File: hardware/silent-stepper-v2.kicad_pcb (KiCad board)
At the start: 4 copper layers, 80 x 80 mm, 112 parts, among them P1 VIN, P101 CON-SENSOR2, P102 DEBUG, P103 BOOT, P2 OUT, P3 GPIO, P4 PROTO, Q1 CSD19533Q5A, Q2 CSD19533Q5A, Q3 CSD19533Q5A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

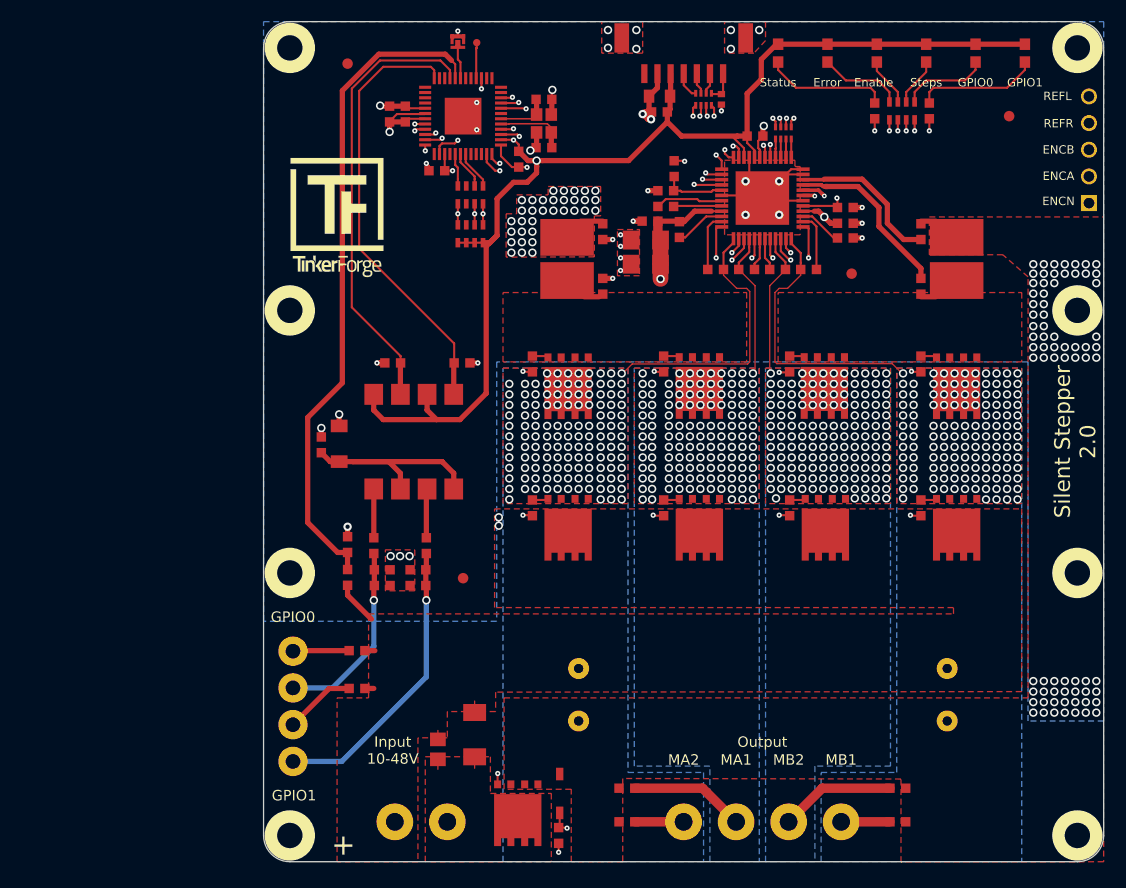
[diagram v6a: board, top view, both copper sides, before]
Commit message: changed shunt resistors
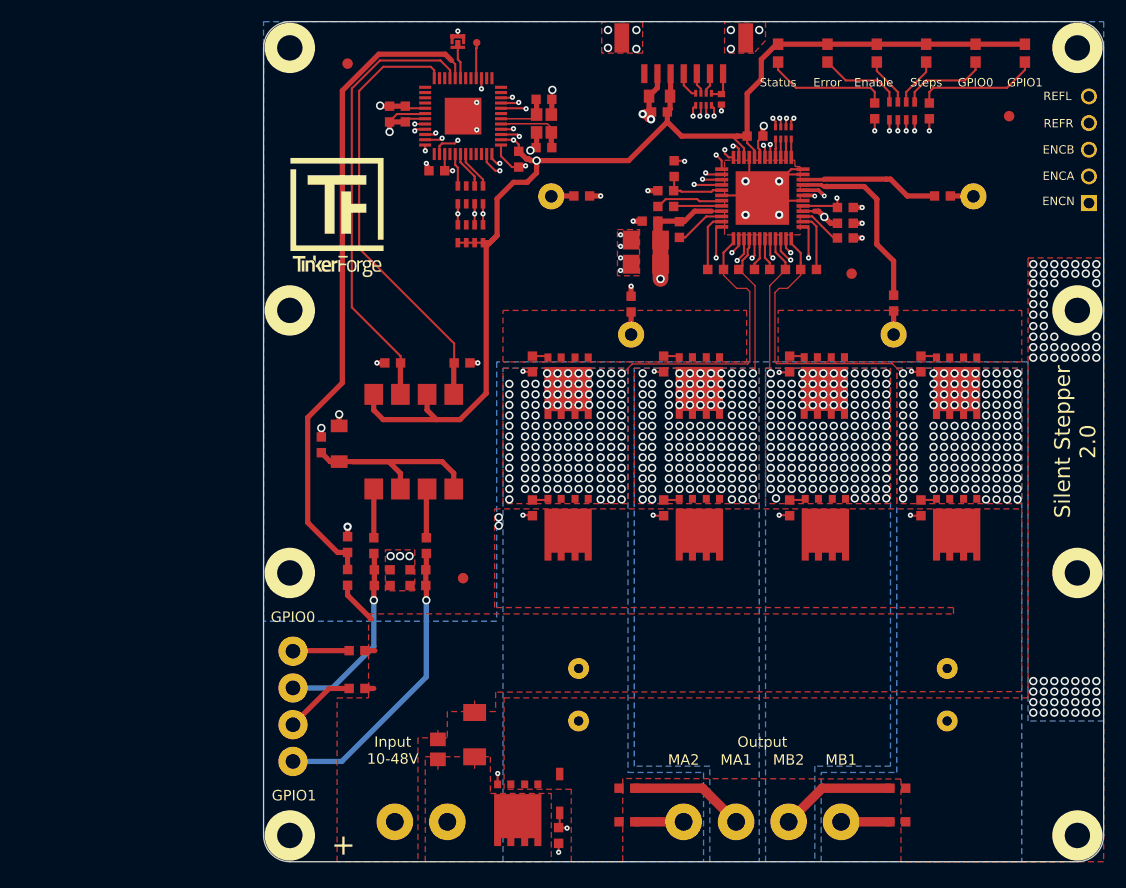
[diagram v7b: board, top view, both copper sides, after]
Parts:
- R10: value WSHM2818R0220FEA -> MRS-3; footprint kicad-libraries:R2818 -> kicad-libraries:MSR-3
- R11: value WSHM2818R0220FEA -> MRS_-3; footprint kicad-libraries:R2818 -> kicad-libraries:MSR-3
- moved R7 3.97 mm to (109.7, 106.6), turned to 180 degrees
- moved R9 3.94 mm to (75.3, 106.6), turned to 0 degrees
- moved R8 3.19 mm to (80.0, 116.9)
- moved R6 3.05 mm to (105.0, 116.8)
- moved R11 2.38 mm to (76.2, 113.2), turned to 300 degrees
- moved R10 2.29 mm to (108.8, 113.2), turned to 240 degrees
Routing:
- net GND: track 67.7 -> 61.5 mm, vias 145 -> 112
- net V_GPIO: track 94.0 -> 97.0 mm
- net Net-(R2-Pad2): track 33.8 -> 36.7 mm
- net Net-(R3-Pad2): track 18.6 -> 21.2 mm
- net Net-(Q4-PadS): track 4.23 -> 2.15 mm
- net Net-(Q2-PadS): track 4.23 -> 2.25 mm
- net Net-(R15-Pad2): track 27.1 -> 28.7 mm
- net Net-(R14-Pad2): track 41.8 -> 43.4 mm
- net Net-(R7-Pad2): track 14.7 -> 13.2 mm
- net Net-(R8-Pad2): track 26.8 -> 25.4 mm
- net Net-(R6-Pad2): track 16.7 -> 17.6 mm
- net Net-(R9-Pad2): track 23.5 -> 22.8 mm

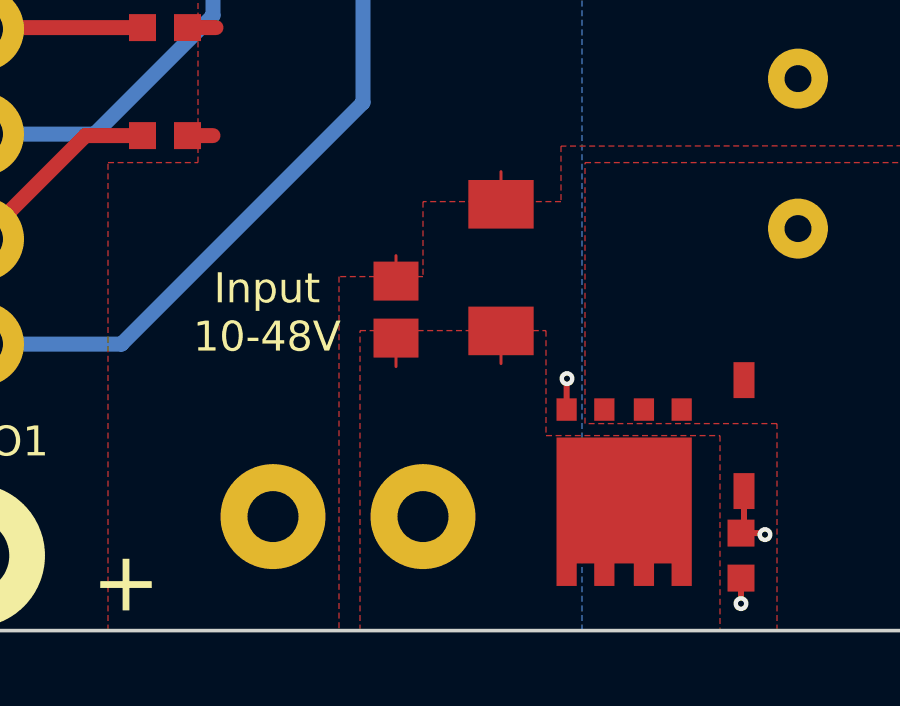
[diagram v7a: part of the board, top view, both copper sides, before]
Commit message: changed varistor value and footprint
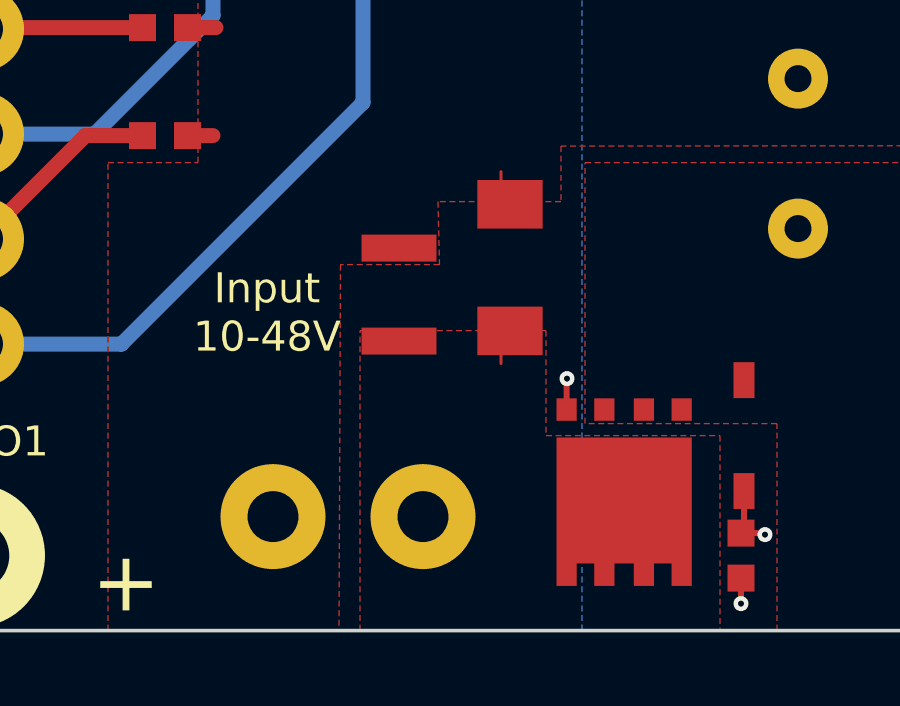
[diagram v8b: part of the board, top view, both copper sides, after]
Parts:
- removed PTC1: VC080526C580DP, kicad-libraries:R0805E
- added R29: VG121048H101DP, kicad-libraries:1210, F.Cu at (61.7, 158.8)
- D8: value SMBJ24CA -> SMBJ48CA
- moved D8 0.30 mm to (65.4, 157.9)
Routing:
- net Net-(D8-Pad2): track 2.04 -> 1.09 mm
- net V_GPIO: track 97.0 -> 96.2 mm
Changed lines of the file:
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@@
     (thickness 1.6)
     (drawings 43)
-    (tracks 1488)
+    (tracks 1486)
     (zones 0)
     (modules 112)
@@
   )
   (setup
-    (last_trace_width 0.5)
+    (last_trace_width 0.1)
     (user_trace_width 0.1)
     (user_trace_width 0.15)
@@
   )
   (module kicad-libraries:SMB (layer F.Cu)
-    (at 65.1 157.9 270)
+    (at 65.4 157.9 270)
     (fp_text reference D8 (at 0 0.5 270) (layer F.Fab)
       (effects (font (size 0.15 0.15) (thickness 0.0375)))
     )
-    (fp_text value SMBJ24CA (at 0.18 -0.575001 270) (layer F.Fab)
+    (fp_text value SMBJ48CA (at 0.18 -0.575001 270) (layer F.Fab)
       (effects (font (size 0.15 0.15) (thickness 0.0375)))
     )
@@
     )
   )
-  (module kicad-libraries:R0805E (layer F.Cu)
-    (at 61.6 159.3 90)
-    (attr smd)
-    (fp_text reference PTC1 (at 0 0.2 90) (layer F.Fab)
-      (effects (font (size 0.2 0.2) (thickness 0.05)))
-    )
-    (fp_text value VC080526C580DP (at 0 -0.4 90) (layer F.Fab)
-      (effects (font (size 0.2 0.2) (thickness 0.05)))
-    )
-    (fp_line (start 1.651 -0.8001) (end -1.651 -0.8001) (layer F.Fab) (width 0.001))
-    (fp_line (start 1.651 0.8001) (end 1.651 -0.8001) (layer F.Fab) (width 0.001))
-    (fp_line (start -1.651 0.8001) (end 1.651 0.8001) (layer F.Fab) (width 0.001))
-    (fp_line (start -1.651 -0.8001) (end -1.651 0.8001) (layer F.Fab) (width 0.001))
-    (pad 2 smd rect (at 0.95 0 90) (size 1.3 1.5) (layers F.Cu F.Paste F.Mask)
-      (net 82 V_GPIO) (clearance 0.14986))
-    (pad 1 smd rect (at -0.95 0 90) (size 1.3 1.5) (layers F.Cu F.Paste F.Mask)
-      (net 114 "Net-(D8-Pad2)") (clearance 0.14986))
-    (model Resistors_SMD/R_0805.wrl
-      (at (xyz 0 0 0))
-      (scale (xyz 1 1 1))
-      (rotate (xyz 0 0 0))
-    )
-  )
   (module kicad-libraries:C1206E (layer F.Cu)
     (at 81.4 110.8 180)
@@
       (net 1 GND))
   )
+  (module kicad-libraries:1210 (layer F.Cu)
+    (at 61.7 158.8 270)
+    (fp_text reference R29 (at 0 0 90) (layer F.Fab)
+      (effects (font (size 0.29972 0.29972) (thickness 0.07493)))
+    )
+    (fp_text value VG121048H101DP (at 0 1.95072 90) (layer F.Fab)
+      (effects (font (size 0.29972 0.29972) (thickness 0.07493)))
+    )
+    (fp_line (start -1.6002 -1.24968) (end -1.6002 1.24968) (layer F.Fab) (width 0.381))
+    (fp_line (start -1.6002 1.24968) (end 1.6002 1.24968) (layer F.Fab) (width 0.381))
+    (fp_line (start 1.6002 1.24968) (end 1.6002 -1.24968) (layer F.Fab) (width 0.381))
+    (fp_line (start 1.6002 -1.24968) (end -1.6002 -1.24968) (layer F.Fab) (width 0.381))
+    (pad 1 smd rect (at -1.5494 0 270) (size 0.89916 2.49936) (layers F.Cu F.Paste F.Mask)
+      (net 82 V_GPIO) (clearance 0.14986))
+    (pad 2 smd rect (at 1.5494 0 270) (size 0.89916 2.49936) (layers F.Cu F.Paste F.Mask)
+      (net 114 "Net-(D8-Pad2)") (clearance 0.14986))
+  )
   (gr_text Output (at 92.5 158.6) (layer F.SilkS)
     (effects (font (size 1 1) (thickness 0.15)))
@@
   (segment (start 98.4 108.6) (end 97.85 108.05) (width 0.5) (layer F.Cu) (net 82))
   (segment (start 97.85 108.05) (end 97.45 108.05) (width 0.5) (layer F.Cu) (net 82))
-  (segment (start 61.6 158.35) (end 61.6 157.5) (width 0.1) (layer F.Cu) (net 82))
   (segment (start 65.1 155.79) (end 65.1 154.7) (width 0.1) (layer F.Cu) (net 82))
   (segment (start 85.05 109.05) (end 86.05 108.05) (width 0.5) (layer F.Cu) (net 82))
@@
   (segment (start 98.550055 95.750055) (end 65.649945 95.750055) (width 0.2) (layer In2.Cu) (net 110))
   (segment (start 65.1 160.01) (end 65.1 161.1) (width 0.1) (layer F.Cu) (net 114))
-  (segment (start 61.6 160.25) (end 61.6 161.2) (width 0.1) (layer F.Cu) (net 114))
   (segment (start 53 142.175) (end 53 140.55) (width 0.5) (layer F.Cu) (net 116))
   (segment (start 63.2507 94.0507) (end 62.9 93.7) (width 0.2) (layer F.Cu) (net 116))
@@
     (polygon
       (pts
-        (xy 117.2 153.8) (xy 67.1 153.85) (xy 67.1 155.7) (xy 62.5 155.7) (xy 62.5 158.2)
-        (xy 59.7 158.2) (xy 59.7 170) (xy 52 170) (xy 52 154.4) (xy 55 154.4)
+        (xy 117.2 153.8) (xy 67.1 153.85) (xy 67.1 155.7) (xy 63 155.7) (xy 63.05 157.8)
+        (xy 59.75 157.8) (xy 59.7 170) (xy 52 170) (xy 52 154.4) (xy 55 154.4)
         (xy 55 146.4) (xy 67.9 146.4) (xy 110.7 146.4) (xy 110.7 145.8) (xy 67 145.8)
         (xy 67 136.4) (xy 117.2 136.4)
